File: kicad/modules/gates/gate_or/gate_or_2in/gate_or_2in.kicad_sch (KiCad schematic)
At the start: 6 parts, among them Q301 NMOS, Q302 PMOS, Q303 PMOS, Q304 NMOS, Q305 PMOS, Q306 NMOS

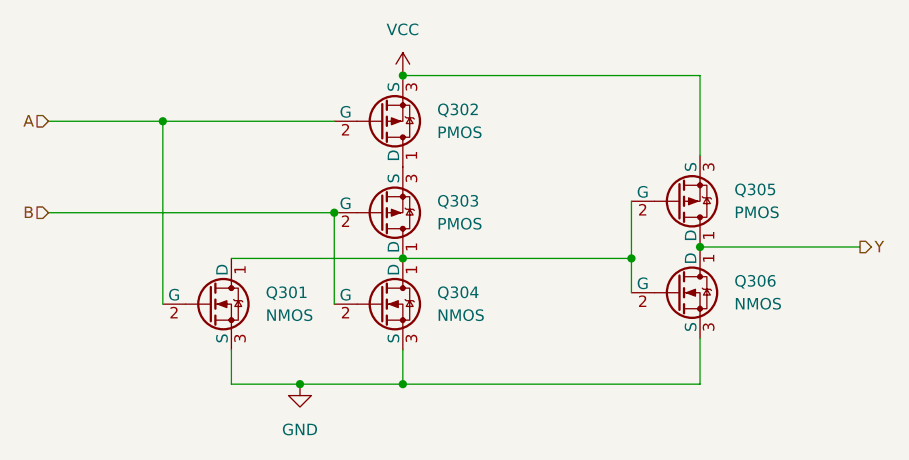
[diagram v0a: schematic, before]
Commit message: feat: complete circuit designs for all ALU components
* Designed all gate modules: AND, OR, NOT, NAND, NOR, XOR (1-bit and 8-bit variants)

* Completed multiplexer hierarchy: 2:1, 4:1, and 8:1 8-bit muxes

* Finalized add_sub board schematic and LED panel designs

* Added new board modules: flags, main_control, main_logic

* Updated Logisim top-level ALU circuit

* Note: KiCad directory path errors to be resolved next (iCloud sync issue), then begin PCB routing
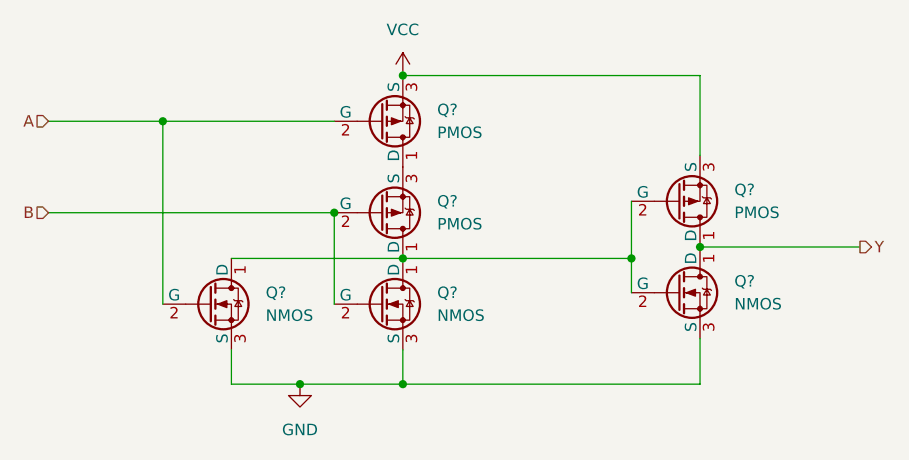
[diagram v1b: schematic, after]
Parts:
- renumbered Q303 to Q?, Q305 to Q?, Q302 to Q?, Q301 to Q?, Q306 to Q?, Q304 to Q?
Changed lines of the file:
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@@
 		(dnp no)
 		(fields_autoplaced yes)
-		(property "Reference" "#PWR0302"
+		(property "Reference" "#PWR?"
 			(at 106.68 63.5 0)
 			(effects
@@
 		)
 		(instances
-			(project "add_sub"
-				(path "/1a086df7-7508-4c0d-b696-2f052ea4c322/077a3c45-851c-4896-9624-dff1a2003e83"
+			(project "led_panel_3"
+				(path "/892e505f-6651-4aa4-9d30-6fa009555436/0e0286f7-35b1-4ca6-892d-2574e85e738d"
+					(reference "#PWR?")
+					(unit 1)
+				)
+				(path "/892e505f-6651-4aa4-9d30-6fa009555436/c9dde3eb-506b-4f3f-9f1d-fa6bf2c8a1c3"
+					(reference "#PWR?")
+					(unit 1)
+				)
+			)
+			(project "main_control"
+				(path "/e2bb65ff-e340-4712-a878-121a5433abf0/1191743b-cc20-4e5c-a37f-35d283fea872"
+					(reference "#PWR0904")
+					(unit 1)
+				)
+				(path "/e2bb65ff-e340-4712-a878-121a5433abf0/5b4c739b-8adf-4c81-b665-49ed29ff7576"
 					(reference "#PWR0902")
 					(unit 1)
 				)
-				(path "/1a086df7-7508-4c0d-b696-2f052ea4c322/6c2fdbbb-142b-4598-91b0-f830ec7a2453"
-					(reference "#PWR0302")
+				(path "/e2bb65ff-e340-4712-a878-121a5433abf0/d97c998c-2e3c-4bec-b0d5-74fb5d901a4c"
+					(reference "#PWR0902")
 					(unit 1)
 				)
@@
 		(dnp no)
 		(fields_autoplaced yes)
-		(property "Reference" "Q303"
+		(property "Reference" "Q?"
 			(at 110.49 73.6599 0)
 			(effects
@@
 		)
 		(instances
-			(project "add_sub"
-				(path "/1a086df7-7508-4c0d-b696-2f052ea4c322/077a3c45-851c-4896-9624-dff1a2003e83"
+			(project "led_panel_3"
+				(path "/892e505f-6651-4aa4-9d30-6fa009555436/0e0286f7-35b1-4ca6-892d-2574e85e738d"
+					(reference "Q?")
+					(unit 1)
+				)
+				(path "/892e505f-6651-4aa4-9d30-6fa009555436/c9dde3eb-506b-4f3f-9f1d-fa6bf2c8a1c3"
+					(reference "Q?")
+					(unit 1)
+				)
+			)
+			(project "main_control"
+				(path "/e2bb65ff-e340-4712-a878-121a5433abf0/1191743b-cc20-4e5c-a37f-35d283fea872"
+					(reference "Q909")
+					(unit 1)
+				)
+				(path "/e2bb65ff-e340-4712-a878-121a5433abf0/5b4c739b-8adf-4c81-b665-49ed29ff7576"
 					(reference "Q903")
 					(unit 1)
 				)
-				(path "/1a086df7-7508-4c0d-b696-2f052ea4c322/6c2fdbbb-142b-4598-91b0-f830ec7a2453"
-					(reference "Q303")
+				(path "/e2bb65ff-e340-4712-a878-121a5433abf0/d97c998c-2e3c-4bec-b0d5-74fb5d901a4c"
+					(reference "Q903")
 					(unit 1)
 				)
@@
 		(dnp no)
 		(fields_autoplaced yes)
-		(property "Reference" "#PWR0301"
+		(property "Reference" "#PWR?"
 			(at 95.25 100.33 0)
 			(effects
@@
 		)
 		(instances
-			(project "add_sub"
-				(path "/1a086df7-7508-4c0d-b696-2f052ea4c322/077a3c45-851c-4896-9624-dff1a2003e83"
+			(project "led_panel_3"
+				(path "/892e505f-6651-4aa4-9d30-6fa009555436/0e0286f7-35b1-4ca6-892d-2574e85e738d"
+					(reference "#PWR?")
+					(unit 1)
+				)
+				(path "/892e505f-6651-4aa4-9d30-6fa009555436/c9dde3eb-506b-4f3f-9f1d-fa6bf2c8a1c3"
+					(reference "#PWR?")
+					(unit 1)
+				)
+			)
+			(project "main_control"
+				(path "/e2bb65ff-e340-4712-a878-121a5433abf0/1191743b-cc20-4e5c-a37f-35d283fea872"
+					(reference "#PWR0903")
+					(unit 1)
+				)
+				(path "/e2bb65ff-e340-4712-a878-121a5433abf0/5b4c739b-8adf-4c81-b665-49ed29ff7576"
 					(reference "#PWR0901")
 					(unit 1)
 				)
-				(path "/1a086df7-7508-4c0d-b696-2f052ea4c322/6c2fdbbb-142b-4598-91b0-f830ec7a2453"
-					(reference "#PWR0301")
+				(path "/e2bb65ff-e340-4712-a878-121a5433abf0/d97c998c-2e3c-4bec-b0d5-74fb5d901a4c"
+					(reference "#PWR0901")
 					(unit 1)
 				)
@@
 		(dnp no)
 		(fields_autoplaced yes)
-		(property "Reference" "Q305"
+		(property "Reference" "Q?"
 			(at 143.51 72.3899 0)
 			(effects
@@
 		)
 		(instances
-			(project "add_sub"
-				(path "/1a086df7-7508-4c0d-b696-2f052ea4c322/077a3c45-851c-4896-9624-dff1a2003e83"
+			(project "led_panel_3"
+				(path "/892e505f-6651-4aa4-9d30-6fa009555436/0e0286f7-35b1-4ca6-892d-2574e85e738d"
+					(reference "Q?")
+					(unit 1)
+				)
+				(path "/892e505f-6651-4aa4-9d30-6fa009555436/c9dde3eb-506b-4f3f-9f1d-fa6bf2c8a1c3"
+					(reference "Q?")
+					(unit 1)
+				)
+			)
+			(project "main_control"
+				(path "/e2bb65ff-e340-4712-a878-121a5433abf0/1191743b-cc20-4e5c-a37f-35d283fea872"
+					(reference "Q911")
+					(unit 1)
+				)
+				(path "/e2bb65ff-e340-4712-a878-121a5433abf0/5b4c739b-8adf-4c81-b665-49ed29ff7576"
 					(reference "Q905")
 					(unit 1)
 				)
-				(path "/1a086df7-7508-4c0d-b696-2f052ea4c322/6c2fdbbb-142b-4598-91b0-f830ec7a2453"
-					(reference "Q305")
+				(path "/e2bb65ff-e340-4712-a878-121a5433abf0/d97c998c-2e3c-4bec-b0d5-74fb5d901a4c"
+					(reference "Q905")
 					(unit 1)
 				)
@@
 		(dnp no)
 		(fields_autoplaced yes)
-		(property "Reference" "Q302"
+		(property "Reference" "Q?"
 			(at 110.49 63.4999 0)
 			(effects
@@
 		)
 		(instances
-			(project "add_sub"
-				(path "/1a086df7-7508-4c0d-b696-2f052ea4c322/077a3c45-851c-4896-9624-dff1a2003e83"
+			(project "led_panel_3"
+				(path "/892e505f-6651-4aa4-9d30-6fa009555436/0e0286f7-35b1-4ca6-892d-2574e85e738d"
+					(reference "Q?")
+					(unit 1)
+				)
+				(path "/892e505f-6651-4aa4-9d30-6fa009555436/c9dde3eb-506b-4f3f-9f1d-fa6bf2c8a1c3"
+					(reference "Q?")
+					(unit 1)
+				)
+			)
+			(project "main_control"
+				(path "/e2bb65ff-e340-4712-a878-121a5433abf0/1191743b-cc20-4e5c-a37f-35d283fea872"
+					(reference "Q908")
+					(unit 1)
+				)
+				(path "/e2bb65ff-e340-4712-a878-121a5433abf0/5b4c739b-8adf-4c81-b665-49ed29ff7576"
 					(reference "Q902")
 					(unit 1)
 				)
-				(path "/1a086df7-7508-4c0d-b696-2f052ea4c322/6c2fdbbb-142b-4598-91b0-f830ec7a2453"
-					(reference "Q302")
+				(path "/e2bb65ff-e340-4712-a878-121a5433abf0/d97c998c-2e3c-4bec-b0d5-74fb5d901a4c"
+					(reference "Q902")
 					(unit 1)
 				)
@@
 		(dnp no)
 		(fields_autoplaced yes)
-		(property "Reference" "Q301"
+		(property "Reference" "Q?"
 			(at 91.44 83.8199 0)
 			(effects
@@
 		)
 		(instances
-			(project "add_sub"
-				(path "/1a086df7-7508-4c0d-b696-2f052ea4c322/077a3c45-851c-4896-9624-dff1a2003e83"
+			(project "led_panel_3"
+				(path "/892e505f-6651-4aa4-9d30-6fa009555436/0e0286f7-35b1-4ca6-892d-2574e85e738d"
+					(reference "Q?")
+					(unit 1)
+				)
+				(path "/892e505f-6651-4aa4-9d30-6fa009555436/c9dde3eb-506b-4f3f-9f1d-fa6bf2c8a1c3"
+					(reference "Q?")
+					(unit 1)
+				)
+			)
+			(project "main_control"
+				(path "/e2bb65ff-e340-4712-a878-121a5433abf0/1191743b-cc20-4e5c-a37f-35d283fea872"
+					(reference "Q907")
+					(unit 1)
+				)
+				(path "/e2bb65ff-e340-4712-a878-121a5433abf0/5b4c739b-8adf-4c81-b665-49ed29ff7576"
 					(reference "Q901")
 					(unit 1)
 				)
-				(path "/1a086df7-7508-4c0d-b696-2f052ea4c322/6c2fdbbb-142b-4598-91b0-f830ec7a2453"
-					(reference "Q301")
+				(path "/e2bb65ff-e340-4712-a878-121a5433abf0/d97c998c-2e3c-4bec-b0d5-74fb5d901a4c"
+					(reference "Q901")
 					(unit 1)
 				)
@@
 		(dnp no)
 		(fields_autoplaced yes)
-		(property "Reference" "Q306"
+		(property "Reference" "Q?"
 			(at 143.51 82.5499 0)
 			(effects
@@
 		)
 		(instances
-			(project "add_sub"
-				(path "/1a086df7-7508-4c0d-b696-2f052ea4c322/077a3c45-851c-4896-9624-dff1a2003e83"
+			(project "led_panel_3"
+				(path "/892e505f-6651-4aa4-9d30-6fa009555436/0e0286f7-35b1-4ca6-892d-2574e85e738d"
+					(reference "Q?")
+					(unit 1)
+				)
+				(path "/892e505f-6651-4aa4-9d30-6fa009555436/c9dde3eb-506b-4f3f-9f1d-fa6bf2c8a1c3"
+					(reference "Q?")
+					(unit 1)
+				)
+			)
+			(project "main_control"
+				(path "/e2bb65ff-e340-4712-a878-121a5433abf0/1191743b-cc20-4e5c-a37f-35d283fea872"
+					(reference "Q912")
+					(unit 1)
+				)
+				(path "/e2bb65ff-e340-4712-a878-121a5433abf0/5b4c739b-8adf-4c81-b665-49ed29ff7576"
 					(reference "Q906")
 					(unit 1)
 				)
-				(path "/1a086df7-7508-4c0d-b696-2f052ea4c322/6c2fdbbb-142b-4598-91b0-f830ec7a2453"
-					(reference "Q306")
+				(path "/e2bb65ff-e340-4712-a878-121a5433abf0/d97c998c-2e3c-4bec-b0d5-74fb5d901a4c"
+					(reference "Q906")
 					(unit 1)
 				)
@@
 		(dnp no)
 		(fields_autoplaced yes)
-		(property "Reference" "Q304"
+		(property "Reference" "Q?"
 			(at 110.49 83.8199 0)
 			(effects
@@
 		)
 		(instances
-			(project "add_sub"
-				(path "/1a086df7-7508-4c0d-b696-2f052ea4c322/077a3c45-851c-4896-9624-dff1a2003e83"
+			(project "led_panel_3"
+				(path "/892e505f-6651-4aa4-9d30-6fa009555436/0e0286f7-35b1-4ca6-892d-2574e85e738d"
+					(reference "Q?")
+					(unit 1)
+				)
+				(path "/892e505f-6651-4aa4-9d30-6fa009555436/c9dde3eb-506b-4f3f-9f1d-fa6bf2c8a1c3"
+					(reference "Q?")
+					(unit 1)
+				)
+			)
+			(project "main_control"
+				(path "/e2bb65ff-e340-4712-a878-121a5433abf0/1191743b-cc20-4e5c-a37f-35d283fea872"
+					(reference "Q910")
+					(unit 1)
+				)
+				(path "/e2bb65ff-e340-4712-a878-121a5433abf0/5b4c739b-8adf-4c81-b665-49ed29ff7576"
 					(reference "Q904")
 					(unit 1)
 				)
-				(path "/1a086df7-7508-4c0d-b696-2f052ea4c322/6c2fdbbb-142b-4598-91b0-f830ec7a2453"
-					(reference "Q304")
-					(unit 1)
-				)
+				(path "/e2bb65ff-e340-4712-a878-121a5433abf0/d97c998c-2e3c-4bec-b0d5-74fb5d901a4c"
+					(reference "Q904")
+					(unit 1)
+				)

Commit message: Fix KiCad file paths and complete core circuit design
- Fixed file path errors across all KiCad schematics and projects
- Completed core circuit designs:
  * Adder and subtractor modules (adder2, adder8)
  * LED panels (led_panel_1) with display circuits
  * Flag LED circuits for status indicators
  * All dependent logic gate modules (AND, OR, NOT, NAND, NOR, XOR)
  * All multiplexer modules (2:1, 4:1, 8:1, 8-bit)
  * Main control board schematics
  * Flags board schematics
- Updated .gitignore to exclude KiCad backups, cache files, and lock files
- Ready for pin placement and routing of control buses, power rails, and inter-board signals
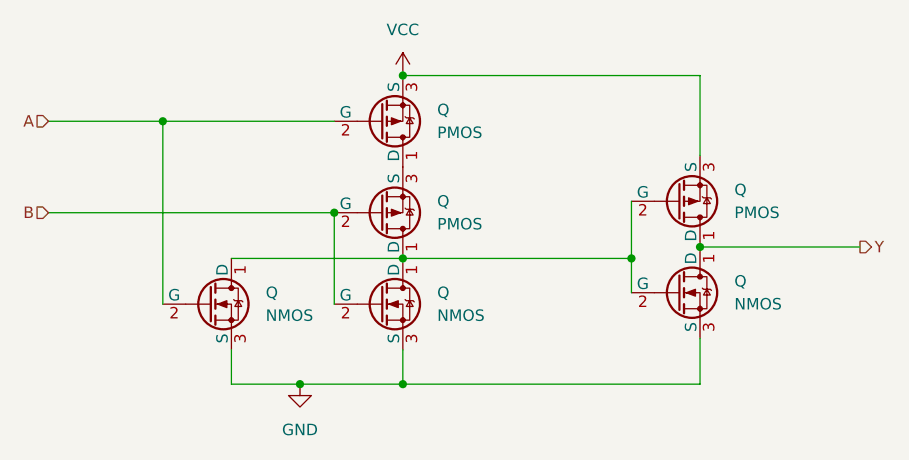
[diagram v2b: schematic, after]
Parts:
- gave numbers to parts that had none: 1
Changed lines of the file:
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@@
 		(dnp no)
 		(fields_autoplaced yes)
-		(property "Reference" "#PWR?"
+		(property "Reference" "#PWR"
 			(at 106.68 63.5 0)
 			(effects
@@
 		)
 		(instances
-			(project "led_panel_3"
-				(path "/892e505f-6651-4aa4-9d30-6fa009555436/0e0286f7-35b1-4ca6-892d-2574e85e738d"
-					(reference "#PWR?")
-					(unit 1)
-				)
-				(path "/892e505f-6651-4aa4-9d30-6fa009555436/c9dde3eb-506b-4f3f-9f1d-fa6bf2c8a1c3"
-					(reference "#PWR?")
-					(unit 1)
-				)
-			)
-			(project "main_control"
-				(path "/e2bb65ff-e340-4712-a878-121a5433abf0/1191743b-cc20-4e5c-a37f-35d283fea872"
-					(reference "#PWR0904")
-					(unit 1)
-				)
-				(path "/e2bb65ff-e340-4712-a878-121a5433abf0/5b4c739b-8adf-4c81-b665-49ed29ff7576"
-					(reference "#PWR0902")
-					(unit 1)
-				)
-				(path "/e2bb65ff-e340-4712-a878-121a5433abf0/d97c998c-2e3c-4bec-b0d5-74fb5d901a4c"
-					(reference "#PWR0902")
+			(project "adder2"
+				(path "/e938a6bb-35cc-48f7-b2cb-f9f5c6ada261/db686d11-0334-4730-a996-2817f62f022c"
+					(reference "#PWR01102")
 					(unit 1)
 				)
@@
 		(dnp no)
 		(fields_autoplaced yes)
-		(property "Reference" "Q?"
+		(property "Reference" "Q"
 			(at 110.49 73.6599 0)
 			(effects
@@
 		)
 		(instances
-			(project "led_panel_3"
-				(path "/892e505f-6651-4aa4-9d30-6fa009555436/0e0286f7-35b1-4ca6-892d-2574e85e738d"
-					(reference "Q?")
-					(unit 1)
-				)
-				(path "/892e505f-6651-4aa4-9d30-6fa009555436/c9dde3eb-506b-4f3f-9f1d-fa6bf2c8a1c3"
-					(reference "Q?")
-					(unit 1)
-				)
-			)
-			(project "main_control"
-				(path "/e2bb65ff-e340-4712-a878-121a5433abf0/1191743b-cc20-4e5c-a37f-35d283fea872"
-					(reference "Q909")
-					(unit 1)
-				)
-				(path "/e2bb65ff-e340-4712-a878-121a5433abf0/5b4c739b-8adf-4c81-b665-49ed29ff7576"
-					(reference "Q903")
-					(unit 1)
-				)
-				(path "/e2bb65ff-e340-4712-a878-121a5433abf0/d97c998c-2e3c-4bec-b0d5-74fb5d901a4c"
-					(reference "Q903")
+			(project "adder2"
+				(path "/e938a6bb-35cc-48f7-b2cb-f9f5c6ada261/db686d11-0334-4730-a996-2817f62f022c"
+					(reference "Q1103")
 					(unit 1)
 				)
@@
 		(dnp no)
 		(fields_autoplaced yes)
-		(property "Reference" "#PWR?"
+		(property "Reference" "#PWR"
 			(at 95.25 100.33 0)
 			(effects
@@
 		)
 		(instances
-			(project "led_panel_3"
-				(path "/892e505f-6651-4aa4-9d30-6fa009555436/0e0286f7-35b1-4ca6-892d-2574e85e738d"
-					(reference "#PWR?")
-					(unit 1)
-				)
-				(path "/892e505f-6651-4aa4-9d30-6fa009555436/c9dde3eb-506b-4f3f-9f1d-fa6bf2c8a1c3"
-					(reference "#PWR?")
-					(unit 1)
-				)
-			)
-			(project "main_control"
-				(path "/e2bb65ff-e340-4712-a878-121a5433abf0/1191743b-cc20-4e5c-a37f-35d283fea872"
-					(reference "#PWR0903")
-					(unit 1)
-				)
-				(path "/e2bb65ff-e340-4712-a878-121a5433abf0/5b4c739b-8adf-4c81-b665-49ed29ff7576"
-					(reference "#PWR0901")
-					(unit 1)
-				)
-				(path "/e2bb65ff-e340-4712-a878-121a5433abf0/d97c998c-2e3c-4bec-b0d5-74fb5d901a4c"
-					(reference "#PWR0901")
+			(project "adder2"
+				(path "/e938a6bb-35cc-48f7-b2cb-f9f5c6ada261/db686d11-0334-4730-a996-2817f62f022c"
+					(reference "#PWR01101")
 					(unit 1)
 				)
@@
 		(dnp no)
 		(fields_autoplaced yes)
-		(property "Reference" "Q?"
+		(property "Reference" "Q"
 			(at 143.51 72.3899 0)
 			(effects
@@
 		)
 		(instances
-			(project "led_panel_3"
-				(path "/892e505f-6651-4aa4-9d30-6fa009555436/0e0286f7-35b1-4ca6-892d-2574e85e738d"
-					(reference "Q?")
-					(unit 1)
-				)
-				(path "/892e505f-6651-4aa4-9d30-6fa009555436/c9dde3eb-506b-4f3f-9f1d-fa6bf2c8a1c3"
-					(reference "Q?")
-					(unit 1)
-				)
-			)
-			(project "main_control"
-				(path "/e2bb65ff-e340-4712-a878-121a5433abf0/1191743b-cc20-4e5c-a37f-35d283fea872"
-					(reference "Q911")
-					(unit 1)
-				)
-				(path "/e2bb65ff-e340-4712-a878-121a5433abf0/5b4c739b-8adf-4c81-b665-49ed29ff7576"
-					(reference "Q905")
-					(unit 1)
-				)
-				(path "/e2bb65ff-e340-4712-a878-121a5433abf0/d97c998c-2e3c-4bec-b0d5-74fb5d901a4c"
-					(reference "Q905")
+			(project "adder2"
+				(path "/e938a6bb-35cc-48f7-b2cb-f9f5c6ada261/db686d11-0334-4730-a996-2817f62f022c"
+					(reference "Q1105")
 					(unit 1)
 				)
@@
 		(dnp no)
 		(fields_autoplaced yes)
-		(property "Reference" "Q?"
+		(property "Reference" "Q"
 			(at 110.49 63.4999 0)
 			(effects
@@
 		)
 		(instances
-			(project "led_panel_3"
-				(path "/892e505f-6651-4aa4-9d30-6fa009555436/0e0286f7-35b1-4ca6-892d-2574e85e738d"
-					(reference "Q?")
-					(unit 1)
-				)
-				(path "/892e505f-6651-4aa4-9d30-6fa009555436/c9dde3eb-506b-4f3f-9f1d-fa6bf2c8a1c3"
-					(reference "Q?")
-					(unit 1)
-				)
-			)
-			(project "main_control"
-				(path "/e2bb65ff-e340-4712-a878-121a5433abf0/1191743b-cc20-4e5c-a37f-35d283fea872"
-					(reference "Q908")
-					(unit 1)
-				)
-				(path "/e2bb65ff-e340-4712-a878-121a5433abf0/5b4c739b-8adf-4c81-b665-49ed29ff7576"
-					(reference "Q902")
-					(unit 1)
-				)
-				(path "/e2bb65ff-e340-4712-a878-121a5433abf0/d97c998c-2e3c-4bec-b0d5-74fb5d901a4c"
-					(reference "Q902")
+			(project "adder2"
+				(path "/e938a6bb-35cc-48f7-b2cb-f9f5c6ada261/db686d11-0334-4730-a996-2817f62f022c"
+					(reference "Q1102")
 					(unit 1)
 				)
@@
 		(dnp no)
 		(fields_autoplaced yes)
-		(property "Reference" "Q?"
+		(property "Reference" "Q"
 			(at 91.44 83.8199 0)
 			(effects
@@
 		)
 		(instances
-			(project "led_panel_3"
-				(path "/892e505f-6651-4aa4-9d30-6fa009555436/0e0286f7-35b1-4ca6-892d-2574e85e738d"
-					(reference "Q?")
-					(unit 1)
-				)
-				(path "/892e505f-6651-4aa4-9d30-6fa009555436/c9dde3eb-506b-4f3f-9f1d-fa6bf2c8a1c3"
-					(reference "Q?")
-					(unit 1)
-				)
-			)
-			(project "main_control"
-				(path "/e2bb65ff-e340-4712-a878-121a5433abf0/1191743b-cc20-4e5c-a37f-35d283fea872"
-					(reference "Q907")
-					(unit 1)
-				)
-				(path "/e2bb65ff-e340-4712-a878-121a5433abf0/5b4c739b-8adf-4c81-b665-49ed29ff7576"
-					(reference "Q901")
-					(unit 1)
-				)
-				(path "/e2bb65ff-e340-4712-a878-121a5433abf0/d97c998c-2e3c-4bec-b0d5-74fb5d901a4c"
-					(reference "Q901")
+			(project "adder2"
+				(path "/e938a6bb-35cc-48f7-b2cb-f9f5c6ada261/db686d11-0334-4730-a996-2817f62f022c"
+					(reference "Q1101")
 					(unit 1)
 				)
@@
 		(dnp no)
 		(fields_autoplaced yes)
-		(property "Reference" "Q?"
+		(property "Reference" "Q"
 			(at 143.51 82.5499 0)
 			(effects
@@
 		)
 		(instances
-			(project "led_panel_3"
-				(path "/892e505f-6651-4aa4-9d30-6fa009555436/0e0286f7-35b1-4ca6-892d-2574e85e738d"
-					(reference "Q?")
-					(unit 1)
-				)
-				(path "/892e505f-6651-4aa4-9d30-6fa009555436/c9dde3eb-506b-4f3f-9f1d-fa6bf2c8a1c3"
-					(reference "Q?")
-					(unit 1)
-				)
-			)
-			(project "main_control"
-				(path "/e2bb65ff-e340-4712-a878-121a5433abf0/1191743b-cc20-4e5c-a37f-35d283fea872"
-					(reference "Q912")
-					(unit 1)
-				)
-				(path "/e2bb65ff-e340-4712-a878-121a5433abf0/5b4c739b-8adf-4c81-b665-49ed29ff7576"
-					(reference "Q906")
-					(unit 1)
-				)
-				(path "/e2bb65ff-e340-4712-a878-121a5433abf0/d97c998c-2e3c-4bec-b0d5-74fb5d901a4c"
-					(reference "Q906")
+			(project "adder2"
+				(path "/e938a6bb-35cc-48f7-b2cb-f9f5c6ada261/db686d11-0334-4730-a996-2817f62f022c"
+					(reference "Q1106")
 					(unit 1)
 				)
@@
 		(dnp no)
 		(fields_autoplaced yes)
-		(property "Reference" "Q?"
+		(property "Reference" "Q"
 			(at 110.49 83.8199 0)
 			(effects
@@
 		)
 		(instances
-			(project "led_panel_3"
-				(path "/892e505f-6651-4aa4-9d30-6fa009555436/0e0286f7-35b1-4ca6-892d-2574e85e738d"
-					(reference "Q?")
-					(unit 1)
-				)
-				(path "/892e505f-6651-4aa4-9d30-6fa009555436/c9dde3eb-506b-4f3f-9f1d-fa6bf2c8a1c3"
-					(reference "Q?")
-					(unit 1)
-				)
-			)
-			(project "main_control"
-				(path "/e2bb65ff-e340-4712-a878-121a5433abf0/1191743b-cc20-4e5c-a37f-35d283fea872"
-					(reference "Q910")
-					(unit 1)
-				)
-				(path "/e2bb65ff-e340-4712-a878-121a5433abf0/5b4c739b-8adf-4c81-b665-49ed29ff7576"
-					(reference "Q904")
-					(unit 1)
-				)
-				(path "/e2bb65ff-e340-4712-a878-121a5433abf0/d97c998c-2e3c-4bec-b0d5-74fb5d901a4c"
-					(reference "Q904")
-					(unit 1)
-				)
+			(project "adder2"
+				(path "/e938a6bb-35cc-48f7-b2cb-f9f5c6ada261/db686d11-0334-4730-a996-2817f62f022c"
+					(reference "Q1104")
+					(unit 1)
+				)
